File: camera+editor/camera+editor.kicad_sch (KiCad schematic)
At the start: 11 parts, among them J1 Micro_SD_Card, Q1 AO3401A, Q2 2N7000, SW1 POWER_SW, SW2 SHUTTER_SW

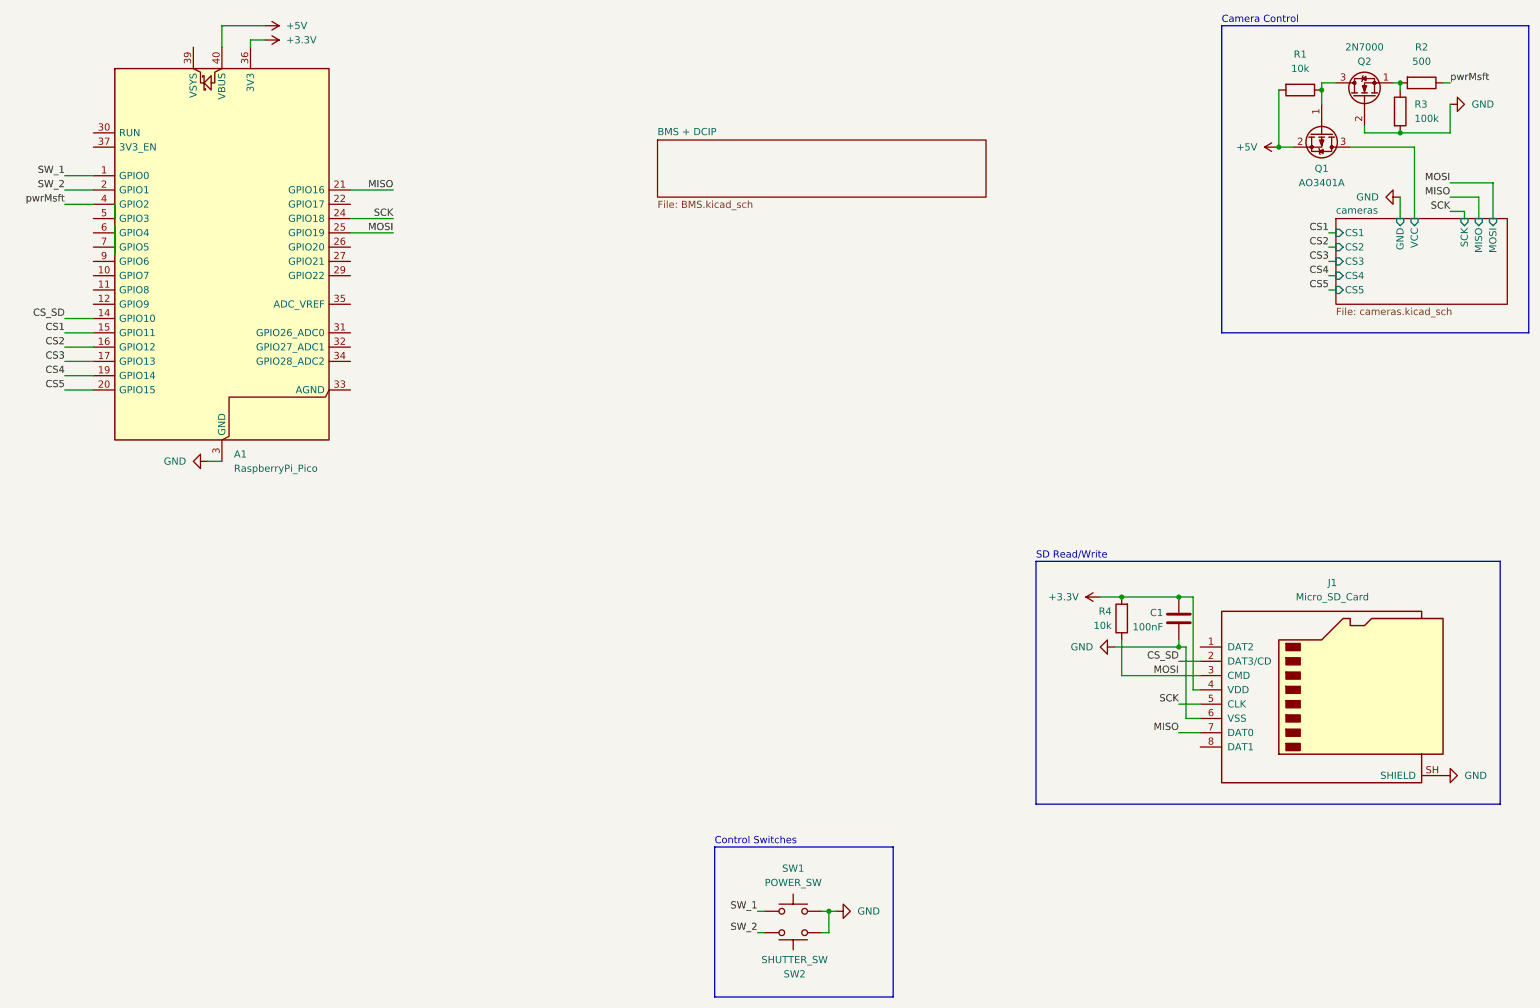
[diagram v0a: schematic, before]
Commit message: pin numbers changed inb frimware, schematic updated
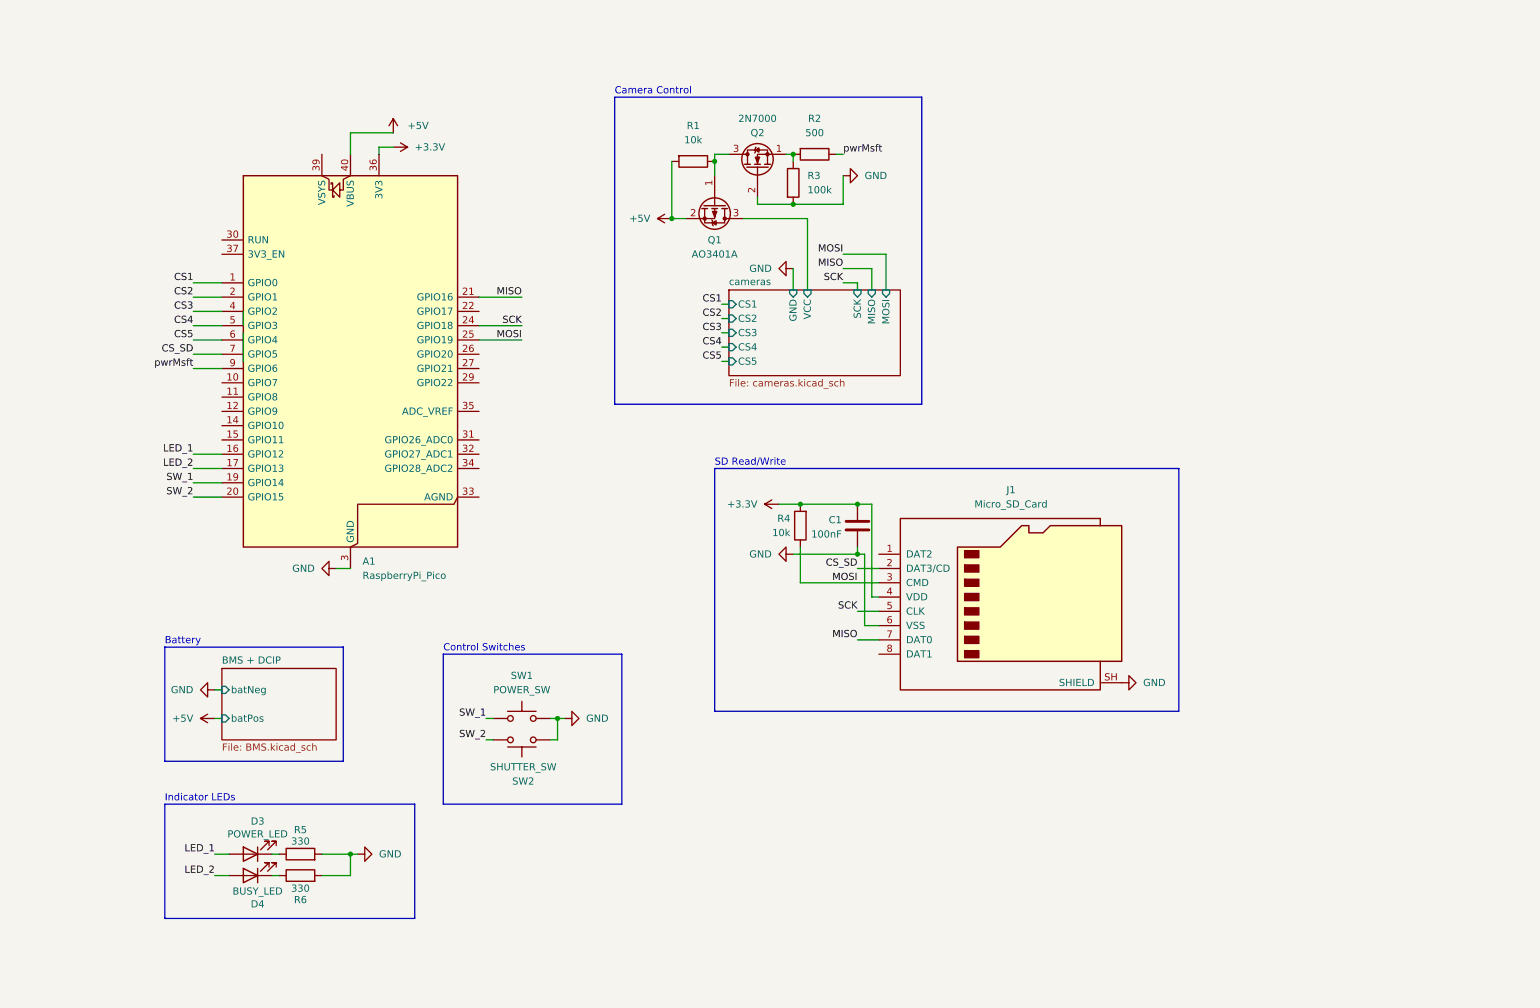
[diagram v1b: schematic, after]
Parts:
- added D3: POWER_LED, symbol Device:LED
- added D4: BUSY_LED, symbol Device:LED
- added R5, R6: 330, symbol Device:R
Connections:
- net CS1: now also A1.1 (GPIO0); no longer A1.15 (GPIO11)
- net CS2: now also A1.2 (GPIO1); no longer A1.16 (GPIO12)
- net CS3: now also A1.4 (GPIO2); no longer A1.17 (GPIO13)
- net CS4: now also A1.5 (GPIO3); no longer A1.19 (GPIO14)
- net CS5: now also A1.6 (GPIO4); no longer A1.20 (GPIO15)
- net CS_SD: now also A1.7 (GPIO5); no longer A1.14 (GPIO10)
- net GND: now also R5.2, R6.2
- net SW_1: now also A1.19 (GPIO14); no longer A1.1 (GPIO0)
- net SW_2: now also A1.20 (GPIO15); no longer A1.2 (GPIO1)
- net pwrMsft: now also A1.9 (GPIO6); no longer A1.4 (GPIO2)
- new net: D4.1 (K), R6.1
- new net: D3.1 (K), R5.1
- new net LED_1: A1.16 (GPIO12), D3.2 (A)
- new net LED_2: A1.17 (GPIO13), D4.2 (A)
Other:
- sheet BMS + DCIP ports: added batNeg, batPos; removed none
- note added: "Battery"
- note added: "Indicator LEDs"
- moved on the sheet: A1, C1, J1, Q1, Q2, R1, R2, R3, R4, SW1, SW2
